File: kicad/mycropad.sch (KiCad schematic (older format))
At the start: 23 parts, among them SW1 SW_Push, SW2 SW_Push, SW3 SW_Push, SW4 SW_Push, SW5 SW_Push, SW6 SW_Push, SW7 SW_Push, SW8 SW_Push, U1 Pico, U2 SN74AHCT125N

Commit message: Even better
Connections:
- net GND: now also U1.13 (GND), U1.18 (GND), U1.3 (GND), U1.42 (GND), U1.8 (GND)
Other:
- note added: "Mycropad board"
- note added: "Neopixel logic shifter"
- note added: "Neopixels"
- note added: "Raspberry PI"
- moved on the sheet: D1, D2, D3, D4, D5, D6, D7, D8, R1, R2, R3, R4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

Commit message: Updated footprints
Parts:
- R1, R2, R3, R4: footprint Resistor_THT:R_Box_L8.4mm_W2.5mm_P5.08mm -> Resistor_THT:R_Axial_DIN0204_L3.6mm_D1.6mm_P5.08mm_Horizontal
- SW1, SW2, SW3, SW4, SW5, SW6, SW7, SW8: footprint macropad:SW_Cherry_MX_1.00u_PCB__Rotated -> mycropad:SW_Cherry_MX_1.00u_PCB__Rotated
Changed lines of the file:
@@
 F 0 "SW3" H 4750 5793 50  0000 C CNN
 F 1 "SW_Push" H 4750 5794 50  0001 C CNN
-F 2 "macropad:SW_Cherry_MX_1.00u_PCB__Rotated" H 4750 5800 50  0001 C CNN
+F 2 "mycropad:SW_Cherry_MX_1.00u_PCB__Rotated" H 4750 5800 50  0001 C CNN
 F 3 "~" H 4750 5800 50  0001 C CNN
 	1    4750 5600
@@
 F 0 "R4" H 5220 3246 50  0000 L CNN
 F 1 "10k" H 5220 3155 50  0000 L CNN
-F 2 "Resistor_THT:R_Box_L8.4mm_W2.5mm_P5.08mm" V 5080 3200 50  0001 C CNN
+F 2 "Resistor_THT:R_Axial_DIN0204_L3.6mm_D1.6mm_P5.08mm_Horizontal" V 5080 3200 50  0001 C CNN
 F 3 "~" H 5150 3200 50  0001 C CNN
 	1    5150 3200
@@
 F 0 "R2" H 1420 5196 50  0000 L CNN
 F 1 "10k" H 1420 5105 50  0000 L CNN
-F 2 "Resistor_THT:R_Box_L8.4mm_W2.5mm_P5.08mm" V 1280 5150 50  0001 C CNN
+F 2 "Resistor_THT:R_Axial_DIN0204_L3.6mm_D1.6mm_P5.08mm_Horizontal" V 1280 5150 50  0001 C CNN
 F 3 "~" H 1350 5150 50  0001 C CNN
 	1    1350 5150
@@
 F 0 "R3" H 1670 5146 50  0000 L CNN
 F 1 "10k" H 1670 5055 50  0000 L CNN
-F 2 "Resistor_THT:R_Box_L8.4mm_W2.5mm_P5.08mm" V 1530 5100 50  0001 C CNN
+F 2 "Resistor_THT:R_Axial_DIN0204_L3.6mm_D1.6mm_P5.08mm_Horizontal" V 1530 5100 50  0001 C CNN
 F 3 "~" H 1600 5100 50  0001 C CNN
 	1    1600 5100
@@
 F 0 "R1" H 3020 5246 50  0000 L CNN
 F 1 "10k" H 3020 5155 50  0000 L CNN
-F 2 "Resistor_THT:R_Box_L8.4mm_W2.5mm_P5.08mm" V 2880 5200 50  0001 C CNN
+F 2 "Resistor_THT:R_Axial_DIN0204_L3.6mm_D1.6mm_P5.08mm_Horizontal" V 2880 5200 50  0001 C CNN
 F 3 "~" H 2950 5200 50  0001 C CNN
 	1    2950 5200
@@
 F 0 "SW7" H 6100 5793 50  0000 C CNN
 F 1 "SW_Push" H 6100 5794 50  0001 C CNN
-F 2 "macropad:SW_Cherry_MX_1.00u_PCB__Rotated" H 6100 5800 50  0001 C CNN
+F 2 "mycropad:SW_Cherry_MX_1.00u_PCB__Rotated" H 6100 5800 50  0001 C CNN
 F 3 "~" H 6100 5800 50  0001 C CNN
 	1    6100 5600
@@
 F 0 "SW8" H 6100 6193 50  0000 C CNN
 F 1 "SW_Push" H 6100 6194 50  0001 C CNN
-F 2 "macropad:SW_Cherry_MX_1.00u_PCB__Rotated" H 6100 6200 50  0001 C CNN
+F 2 "mycropad:SW_Cherry_MX_1.00u_PCB__Rotated" H 6100 6200 50  0001 C CNN
 F 3 "~" H 6100 6200 50  0001 C CNN
 	1    6100 6000
@@
 F 0 "SW6" H 6100 5393 50  0000 C CNN
 F 1 "SW_Push" H 6100 5394 50  0001 C CNN
-F 2 "macropad:SW_Cherry_MX_1.00u_PCB__Rotated" H 6100 5400 50  0001 C CNN
+F 2 "mycropad:SW_Cherry_MX_1.00u_PCB__Rotated" H 6100 5400 50  0001 C CNN
 F 3 "~" H 6100 5400 50  0001 C CNN
 	1    6100 5200
@@
 F 0 "SW5" H 6100 4993 50  0000 C CNN
 F 1 "SW_Push" H 6100 4994 50  0001 C CNN
-F 2 "macropad:SW_Cherry_MX_1.00u_PCB__Rotated" H 6100 5000 50  0001 C CNN
+F 2 "mycropad:SW_Cherry_MX_1.00u_PCB__Rotated" H 6100 5000 50  0001 C CNN
 F 3 "~" H 6100 5000 50  0001 C CNN
 	1    6100 4800
@@
 F 0 "SW4" H 4750 6193 50  0000 C CNN
 F 1 "SW_Push" H 4750 6194 50  0001 C CNN
-F 2 "macropad:SW_Cherry_MX_1.00u_PCB__Rotated" H 4750 6200 50  0001 C CNN
+F 2 "mycropad:SW_Cherry_MX_1.00u_PCB__Rotated" H 4750 6200 50  0001 C CNN
 F 3 "~" H 4750 6200 50  0001 C CNN
 	1    4750 6000
@@
 F 0 "SW1" H 4750 4993 50  0000 C CNN
 F 1 "SW_Push" H 4750 4994 50  0001 C CNN
-F 2 "macropad:SW_Cherry_MX_1.00u_PCB__Rotated" H 4750 5000 50  0001 C CNN
+F 2 "mycropad:SW_Cherry_MX_1.00u_PCB__Rotated" H 4750 5000 50  0001 C CNN
 F 3 "~" H 4750 5000 50  0001 C CNN
 	1    4750 4800
@@
 F 0 "SW2" H 4750 5393 50  0000 C CNN
 F 1 "SW_Push" H 4750 5394 50  0001 C CNN
-F 2 "macropad:SW_Cherry_MX_1.00u_PCB__Rotated" H 4750 5400 50  0001 C CNN
+F 2 "mycropad:SW_Cherry_MX_1.00u_PCB__Rotated" H 4750 5400 50  0001 C CNN
 F 3 "~" H 4750 5400 50  0001 C CNN
 	1    4750 5200
@@
 Mycropad board
 $Comp
-L power:GND #PWR?
+L power:GND #PWR0137
 U 1 1 616CAC02
 P 2500 3550
-F 0 "#PWR?" H 2500 3300 50  0001 C CNN
+F 0 "#PWR0137" H 2500 3300 50  0001 C CNN
 F 1 "GND" V 2505 3422 50  0000 R CNN
 F 2 "" H 2500 3550 50  0001 C CNN

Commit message: Moved around some things
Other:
- moved on the sheet: R1, R2
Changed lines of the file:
@@
 	1650 5850 1650 5450
 Wire Wire Line
-	2550 5350 2950 5350
-Wire Wire Line
-	2950 5050 2950 4850
+	2950 4950 2950 4850
 Wire Wire Line
 	2950 4850 3000 4850
-Wire Wire Line
-	1350 5000 1350 4850
-Wire Wire Line
-	1350 4850 1600 4850
 Connection ~ 2950 4850
 Wire Wire Line
@@
 	1600 5350 1950 5350
 Wire Wire Line
-	1950 5550 1350 5550
-Wire Wire Line
-	1350 5550 1350 5300
+	1300 5550 1300 5250
 Text GLabel 1100 5350 0    50   Output ~ 0
 GPIO17
@@
 	1600 5350 1100 5350
 Connection ~ 1600 5350
-Wire Wire Line
-	1350 5550 1100 5550
-Connection ~ 1350 5550
-Wire Wire Line
-	2950 5350 3350 5350
-Connection ~ 2950 5350
+Connection ~ 1300 5550
 Text GLabel 1200 1550 0    50   Input ~ 0
 GPIO1
@@
 L Device:R R2
 U 1 1 6162DA9A
-P 1350 5150
-F 0 "R2" H 1420 5196 50  0000 L CNN
-F 1 "10k" H 1420 5105 50  0000 L CNN
-F 2 "Resistor_THT:R_Axial_DIN0204_L3.6mm_D1.6mm_P5.08mm_Horizontal" V 1280 5150 50  0001 C CNN
-F 3 "~" H 1350 5150 50  0001 C CNN
-	1    1350 5150
+P 1300 5100
+F 0 "R2" H 1370 5146 50  0000 L CNN
+F 1 "10k" H 1370 5055 50  0000 L CNN
+F 2 "Resistor_THT:R_Axial_DIN0204_L3.6mm_D1.6mm_P5.08mm_Horizontal" V 1230 5100 50  0001 C CNN
+F 3 "~" H 1300 5100 50  0001 C CNN
+	1    1300 5100
 	1    0    0    -1
 $EndComp
@@
 L Device:R R1
 U 1 1 6162CB4D
-P 2950 5200
-F 0 "R1" H 3020 5246 50  0000 L CNN
-F 1 "10k" H 3020 5155 50  0000 L CNN
-F 2 "Resistor_THT:R_Axial_DIN0204_L3.6mm_D1.6mm_P5.08mm_Horizontal" V 2880 5200 50  0001 C CNN
-F 3 "~" H 2950 5200 50  0001 C CNN
-	1    2950 5200
+P 2950 5100
+F 0 "R1" H 3020 5146 50  0000 L CNN
+F 1 "10k" H 3020 5055 50  0000 L CNN
+F 2 "Resistor_THT:R_Axial_DIN0204_L3.6mm_D1.6mm_P5.08mm_Horizontal" V 2880 5100 50  0001 C CNN
+F 3 "~" H 2950 5100 50  0001 C CNN
+	1    2950 5100
 	1    0    0    -1
 $EndComp
@@
 	1    0    0    -1
 $EndComp
-Text GLabel 6050 3050 2    50   Output ~ 0
-NEOPIX_5v
 Wire Wire Line
 	5150 3050 5350 3050
@@
 U 1 1 61931135
 P 5750 2050
-F 0 "U2" H 5700 2953 60  0000 C CNN
-F 1 "SN74AHCT125N" H 5700 2847 60  0000 C CNN
+F 0 "U2" H 5550 2900 60  0000 C CNN
+F 1 "SN74AHCT125N" H 5250 2800 60  0000 C CNN
 F 2 "digikey-footprints:DIP-14_W3mm" H 5950 2250 60  0001 L CNN
 F 3 "http://www.ti.com/general/docs/suppproductinfo.tsp?distId=10&gotoUrl=http%3A%2F%2Fwww.ti.com%2Flit%2Fgpn%2Fsn74ahct125" H 5950 2350 60  0001 L CNN
@@
 Text Notes 10400 4300 2    50   ~ 0
 Neopixels
-Wire Notes Line
-	6700 3350 6700 1550
 Text Notes 2850 4050 2    50   ~ 0
 Raspberry PI
@@
 	-1   0    0    -1
 $EndComp
+Wire Wire Line
+	2550 5350 2950 5350
+Wire Wire Line
+	2950 5250 2950 5350
+Connection ~ 2950 5350
+Wire Wire Line
+	2950 5350 3350 5350
+Wire Wire Line
+	1300 5550 1100 5550
+Wire Wire Line
+	1300 5550 1950 5550
+Wire Wire Line
+	1300 4950 1300 4850
+Wire Wire Line
+	1300 4850 1600 4850
+Text GLabel 6050 3050 2    50   Output ~ 0
+NEOPIX_5v
 $EndSCHEMATC

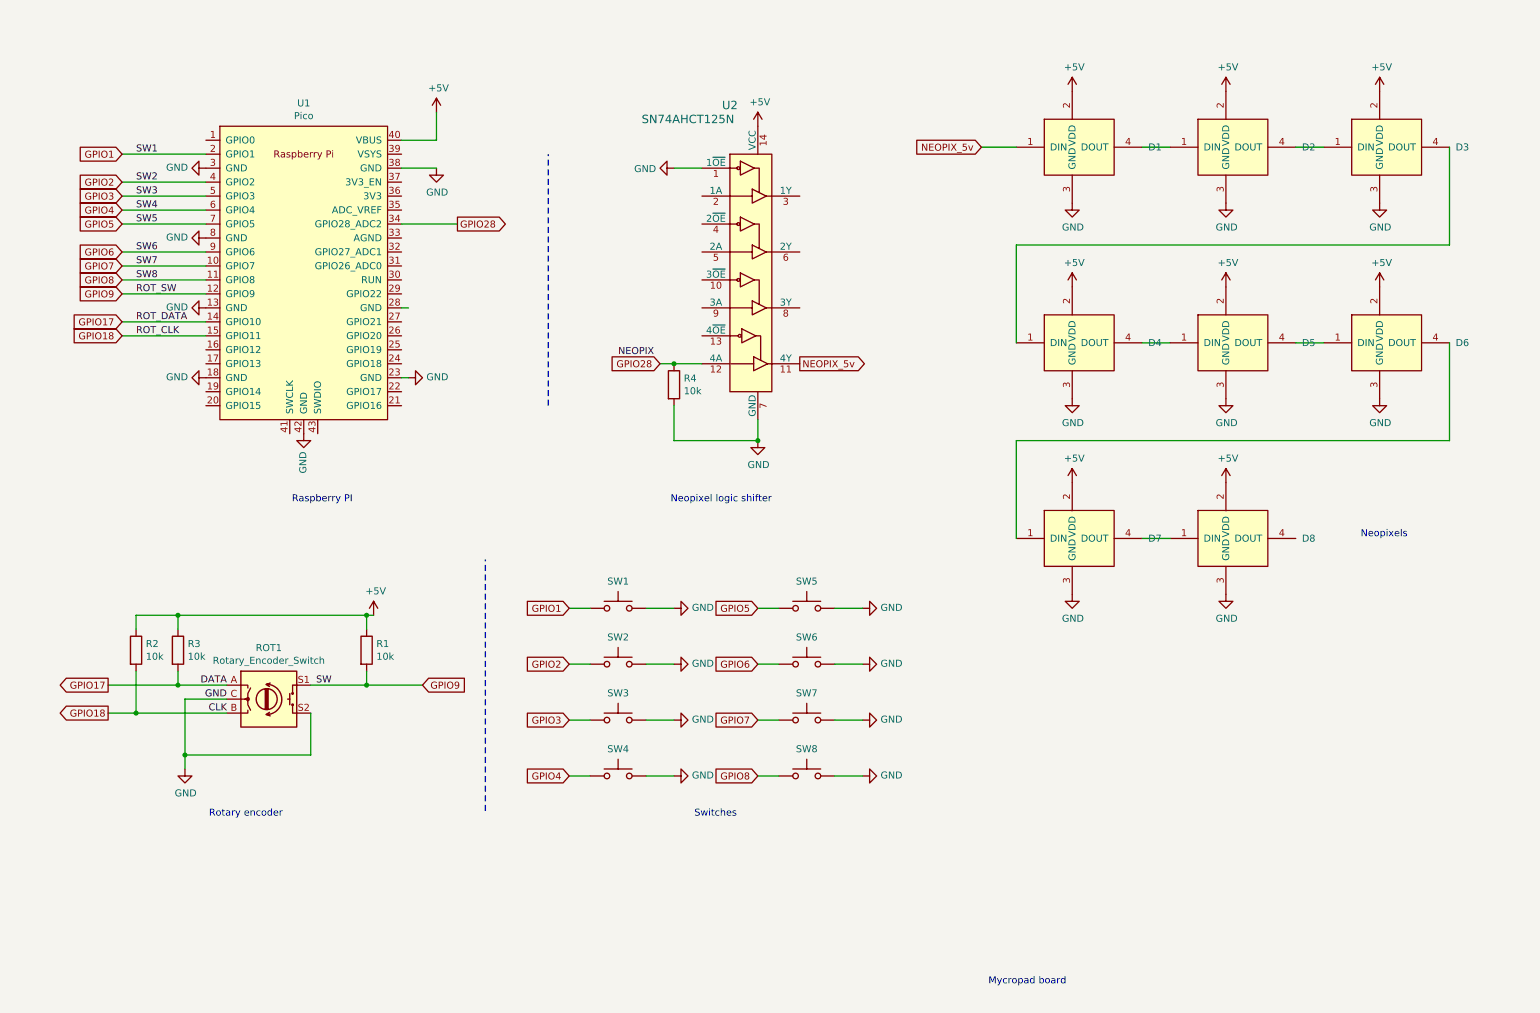
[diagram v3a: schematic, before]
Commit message: Removed useless resistors, PCB design fixes.
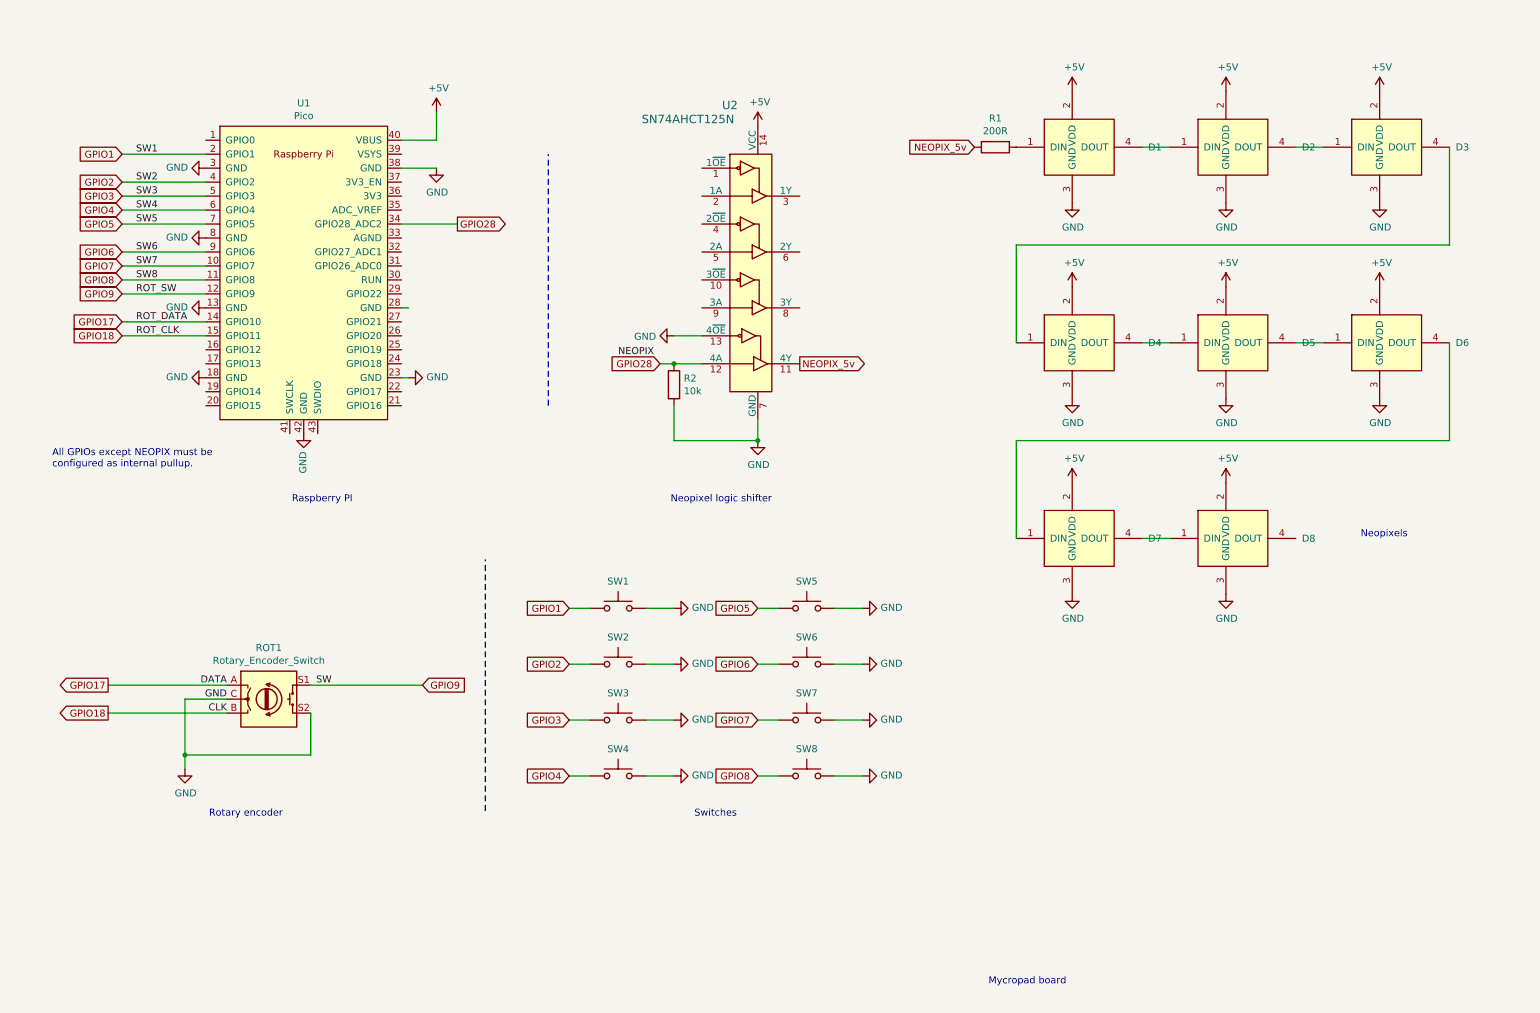
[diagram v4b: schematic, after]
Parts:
- removed R2, R3: 10k, Resistor_THT:R_Axial_DIN0204_L3.6mm_D1.6mm_P5.08mm_Horizontal, symbol Device:R
- R1: value 10k -> 200R
- renumbered R4 to R2
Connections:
- net +5V: no longer R1.1
- net GND: now also U2.13 (4~OE); no longer U2.1 (1~OE)
- net GPIO9: no longer R1.2
- net NEOPIX_5v: now also R1.2; no longer D1.1 (DIN)
- new net: D1.1 (DIN), R1.1
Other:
- note added: "All GPIOs except NEOPIX must be \nconfigured as internal pullup."
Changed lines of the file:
@@
 Wire Wire Line
 	1650 5850 1650 5450
-Wire Wire Line
-	2950 4950 2950 4850
-Wire Wire Line
-	2950 4850 3000 4850
-Connection ~ 2950 4850
-Wire Wire Line
-	1600 4950 1600 4850
-Connection ~ 1600 4850
-Wire Wire Line
-	1600 4850 2950 4850
 Text Label 1950 5550 2    50   ~ 0
 CLK
@@
 Text Label 2700 5350 2    50   ~ 0
 SW
-Wire Wire Line
-	1600 5250 1600 5350
-Wire Wire Line
-	1600 5350 1950 5350
-Wire Wire Line
-	1300 5550 1300 5250
 Text GLabel 1100 5350 0    50   Output ~ 0
 GPIO17
@@
 Text GLabel 3350 5350 2    50   Input ~ 0
 GPIO9
-Wire Wire Line
-	1600 5350 1100 5350
-Connection ~ 1600 5350
-Connection ~ 1300 5550
 Text GLabel 1200 1550 0    50   Input ~ 0
 GPIO1
@@
 Text Notes 5600 6300 2    50   ~ 0
 Switches
-$Comp
-L power:+5V #PWR0104
-U 1 1 6173F12D
-P 3000 4850
-F 0 "#PWR0104" H 3000 4700 50  0001 C CNN
-F 1 "+5V" H 3015 5023 50  0000 C CNN
-F 2 "" H 3000 4850 50  0001 C CNN
-F 3 "" H 3000 4850 50  0001 C CNN
-	1    3000 4850
-	1    0    0    -1
-$EndComp
 Wire Notes Line
 	4250 3350 4250 1550
@@
 	1    0    0    -1
 $EndComp
-Text GLabel 7350 1500 0    50   Input ~ 0
+Text GLabel 7300 1500 0    50   Input ~ 0
 NEOPIX_5v
-Wire Wire Line
-	7350 1500 7600 1500
-$Comp
-L Device:R R4
+$Comp
+L Device:R R2
 U 1 1 6173190B
 P 5150 3200
-F 0 "R4" H 5220 3246 50  0000 L CNN
+F 0 "R2" H 5220 3246 50  0000 L CNN
 F 1 "10k" H 5220 3155 50  0000 L CNN
 F 2 "Resistor_THT:R_Axial_DIN0204_L3.6mm_D1.6mm_P5.08mm_Horizontal" V 5080 3200 50  0001 C CNN
 F 3 "~" H 5150 3200 50  0001 C CNN
 	1    5150 3200
-	1    0    0    -1
-$EndComp
-$Comp
-L Device:R R2
-U 1 1 6162DA9A
-P 1300 5100
-F 0 "R2" H 1370 5146 50  0000 L CNN
-F 1 "10k" H 1370 5055 50  0000 L CNN
-F 2 "Resistor_THT:R_Axial_DIN0204_L3.6mm_D1.6mm_P5.08mm_Horizontal" V 1230 5100 50  0001 C CNN
-F 3 "~" H 1300 5100 50  0001 C CNN
-	1    1300 5100
-	1    0    0    -1
-$EndComp
-$Comp
-L Device:R R3
-U 1 1 6162E01A
-P 1600 5100
-F 0 "R3" H 1670 5146 50  0000 L CNN
-F 1 "10k" H 1670 5055 50  0000 L CNN
-F 2 "Resistor_THT:R_Axial_DIN0204_L3.6mm_D1.6mm_P5.08mm_Horizontal" V 1530 5100 50  0001 C CNN
-F 3 "~" H 1600 5100 50  0001 C CNN
-	1    1600 5100
-	1    0    0    -1
-$EndComp
-$Comp
-L Device:R R1
-U 1 1 6162CB4D
-P 2950 5100
-F 0 "R1" H 3020 5146 50  0000 L CNN
-F 1 "10k" H 3020 5055 50  0000 L CNN
-F 2 "Resistor_THT:R_Axial_DIN0204_L3.6mm_D1.6mm_P5.08mm_Horizontal" V 2880 5100 50  0001 C CNN
-F 3 "~" H 2950 5100 50  0001 C CNN
-	1    2950 5100
 	1    0    0    -1
 $EndComp
@@
 Text Label 4750 3000 0    50   ~ 0
 NEOPIX
-$Comp
-L power:GND #PWR0129
-U 1 1 619569BC
-P 5150 1650
-F 0 "#PWR0129" H 5150 1400 50  0001 C CNN
-F 1 "GND" V 5155 1522 50  0000 R CNN
-F 2 "" H 5150 1650 50  0001 C CNN
-F 3 "" H 5150 1650 50  0001 C CNN
-	1    5150 1650
-	0    1    1    0
-$EndComp
-Wire Wire Line
-	5150 1650 5350 1650
 $Comp
 L Switch:SW_Push SW5
@@
 $EndComp
 Wire Wire Line
-	2550 5350 2950 5350
-Wire Wire Line
-	2950 5250 2950 5350
-Connection ~ 2950 5350
-Wire Wire Line
-	2950 5350 3350 5350
-Wire Wire Line
-	1300 5550 1100 5550
-Wire Wire Line
-	1300 5550 1950 5550
-Wire Wire Line
-	1300 4950 1300 4850
-Wire Wire Line
-	1300 4850 1600 4850
+	5150 2850 5350 2850
+$Comp
+L power:GND #PWR0129
+U 1 1 619569BC
+P 5150 2850
+F 0 "#PWR0129" H 5150 2600 50  0001 C CNN
+F 1 "GND" V 5155 2722 50  0000 R CNN
+F 2 "" H 5150 2850 50  0001 C CNN
+F 3 "" H 5150 2850 50  0001 C CNN
+	1    5150 2850
+	0    1    1    0
+$EndComp
 Text GLabel 6050 3050 2    50   Output ~ 0
 NEOPIX_5v
+Wire Wire Line
+	2550 5350 3350 5350
+Wire Wire Line
+	1100 5550 1950 5550
+Wire Wire Line
+	1100 5350 1950 5350
+Text Notes 700  3800 0    50   ~ 0
+All GPIOs except NEOPIX must be \nconfigured as internal pullup.
+$Comp
+L Device:R R1
+U 1 1 617F32B4
+P 7450 1500
+F 0 "R1" V 7243 1500 50  0000 C CNN
+F 1 "200R" V 7334 1500 50  0000 C CNN
+F 2 "Resistor_THT:R_Axial_DIN0204_L3.6mm_D1.6mm_P5.08mm_Horizontal" V 7380 1500 50  0001 C CNN
+F 3 "~" H 7450 1500 50  0001 C CNN
+	1    7450 1500
+	0    1    1    0
+$EndComp
 $EndSCHEMATC

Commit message: Restored original RPi SMD footprint
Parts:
- U1: footprint macropad:RPi_Pico_SMD_TH -> mycropad:RPi_Pico_SMD_TH
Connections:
- net GPIO9: now also ROT1.B; no longer ROT1.S1
- net GPIO17 renamed GPIO10
- net GPIO18 renamed GPIO11
- net GPIO11: now also ROT1.S1; no longer ROT1.B
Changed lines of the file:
@@
 Text Label 2700 5350 2    50   ~ 0
 SW
-Text GLabel 1100 5350 0    50   Output ~ 0
-GPIO17
-Text GLabel 1100 5550 0    50   Output ~ 0
-GPIO18
-Text GLabel 3350 5350 2    50   Input ~ 0
+Text GLabel 1100 5350 0    50   Input ~ 0
+GPIO10
+Text GLabel 2850 5350 2    50   Input ~ 0
+GPIO11
+Text GLabel 1100 5550 0    50   Input ~ 0
 GPIO9
 Text GLabel 1200 1550 0    50   Input ~ 0
@@
 Text Label 1300 2450 0    50   ~ 0
 SW8
-Text Label 1300 2550 0    50   ~ 0
+Text Label 1300 2850 0    50   ~ 0
 ROT_SW
 Wire Wire Line
@@
 GPIO9
 Text GLabel 1200 2850 0    50   Input ~ 0
-GPIO18
+GPIO11
 Text GLabel 1200 2750 0    50   Input ~ 0
-GPIO17
+GPIO10
 Wire Notes Line
 	3800 6250 3800 4450
@@
 Text Label 1300 2750 0    50   ~ 0
 ROT_DATA
-Text Label 1300 2850 0    50   ~ 0
+Text Label 1300 2550 0    50   ~ 0
 ROT_CLK
 Text GLabel 3600 2050 2    50   Output ~ 0
@@
 F 0 "U1" H 2500 3615 50  0000 C CNN
 F 1 "Pico" H 2500 3524 50  0000 C CNN
-F 2 "macropad:RPi_Pico_SMD_TH" V 2500 2400 50  0001 C CNN
+F 2 "mycropad:RPi_Pico_SMD_TH" V 2500 2400 50  0001 C CNN
 F 3 "" H 2500 2400 50  0001 C CNN
 	1    2500 2400
@@
 NEOPIX_5v
 Wire Wire Line
-	2550 5350 3350 5350
-Wire Wire Line
 	1100 5550 1950 5550
 Wire Wire Line
@@
 	0    1    1    0
 $EndComp
+Wire Wire Line
+	2550 5350 2850 5350
 $EndSCHEMATC

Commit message: New reverse mount led. Let's hope it works...
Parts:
- removed D1, D2, D3, D4, D5, D6, D7, D8: COM-12999, LED_THT:LED_D5.0mm-4_RGB, symbol dk_Addressable-Specialty:COM-12999
- added C1, C2, C3, C4, C5, C6, C7, C8: 10uF, Capacitor_SMD:C_1206_3216Metric_Pad1.33x1.80mm_HandSolder, symbol Device:C
- added D1, D2, D3, D4, D5, D6, D7, D8: SK6812MINI-E, mycropad:LED_SK6812MINI-E_REV02_PLCC4_3.5x3.5mm_P1.75mm, symbol Mycropad:SK6812MINI-E
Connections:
- net +5V: now also C1.2, C2.2, C3.2, C4.2, C5.2, C6.2, C7.2, C8.2, D1.1 (VDD), D2.1 (VDD), D3.1 (VDD), D4.1 (VDD), D5.1 (VDD), D6.1 (VDD), D7.1 (VDD), D8.1 (VDD)
- net GND: now also C1.1, C2.1, C3.1, C4.1, C5.1, C6.1, C7.1, C8.1, D1.3 (VSS), D2.3 (VSS), D3.3 (VSS), D4.3 (VSS), D5.3 (VSS), D6.3 (VSS), D7.3 (VSS), D8.3 (VSS)
- net at R1.1: now also D1.4 (DIN)
- new net: D1.2 (DOUT), D2.4 (DIN)
- new net: D2.2 (DOUT), D3.4 (DIN)
- new net: D3.2 (DOUT), D4.4 (DIN)
- new net: D4.2 (DOUT), D5.4 (DIN)
- new net: D5.2 (DOUT), D6.4 (DIN)
- new net: D6.2 (DOUT), D7.4 (DIN)
- new net: D7.2 (DOUT), D8.4 (DIN)
- no-connect marks 0 -> 34
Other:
- moved on the sheet: R1
